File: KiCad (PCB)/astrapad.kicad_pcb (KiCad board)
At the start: 2 copper layers, 106.9 x 53.6 mm, 34 parts, among them J1 OLED_DISPLAY, SW1 SW_Push, SW13 RotaryEncoder_Switch, SW2 SW_Push, SW3 SW_Push, SW5 SW_Push, SW6 SW_Push, SW7 SW_Push, SW8 SW_Push, U1 XIAO-RP2040-DIP

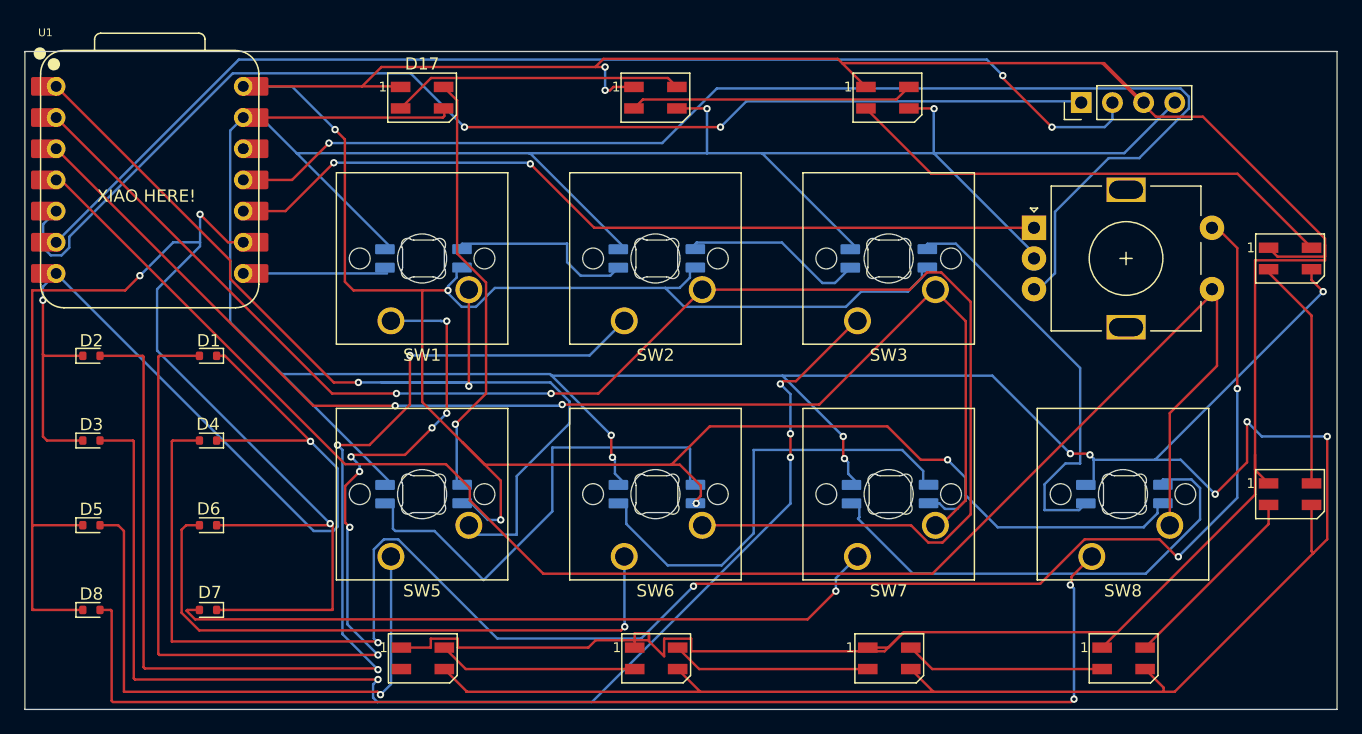
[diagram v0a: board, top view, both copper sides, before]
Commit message: Resized PCB to fit 100mmx100mm limit Turns out the PCB has a max size of 100mmx100mm, mine was 106x59. I resized it though so we good now
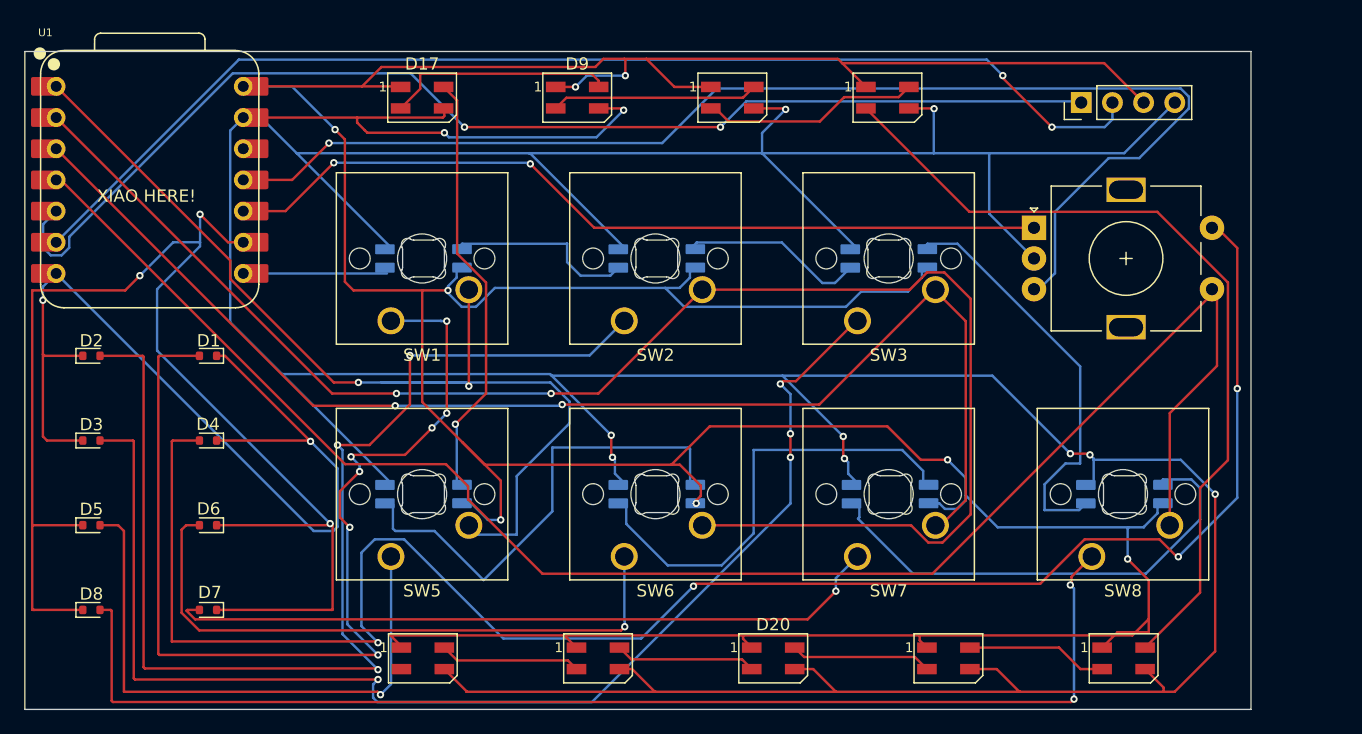
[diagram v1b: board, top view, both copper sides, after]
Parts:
- removed D21: WS2812B, LED_SMD:LED_SK6812MINI_PLCC4_3.5x3.5mm_P1.75mm
- added D9: WS2812B, LED_SMD:LED_SK6812MINI_PLCC4_3.5x3.5mm_P1.75mm, F.Cu at (45.0, 3.76)
- moved D20 53.2 mm to (61.0, 49.4)
- moved D18 6.26 mm to (57.6, 3.76)
- moved D23 4.82 mm to (75.2, 49.4)
- moved D24 4.74 mm to (46.7, 49.4)
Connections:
- D18 pad 4: Net-(D17-DOUT) -> Net-(D18-DIN)
- D20 pad 4: Net-(D19-DOUT) -> Net-(D20-DIN)
- D22 pad 4: Net-(D21-DOUT) -> Net-(D19-DOUT)
- D23 pad 2: Net-(D23-DOUT) -> Net-(D20-DIN)
- D24 pad 4: Net-(D23-DOUT) -> Net-(D20-DOUT)
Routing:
- net +5V: track 410.1 -> 352.5 mm, vias 7 -> 8
- net Net-(D19-DOUT): track 41.0 -> 67.9 mm
- net Net-(D18-DIN): track 0.00 -> 16.9 mm
- net Net-(D23-DOUT): track 16.2 -> 0.00 mm
- net GND: track 426.7 -> 410.6 mm, vias 12 -> 11
- net Net-(D21-DOUT): track 15.8 -> 0.00 mm
- net Net-(D20-DIN): track 0.00 -> 11.5 mm
- net Net-(D20-DOUT): track 19.3 -> 11.5 mm
- net Net-(D18-DOUT): track 23.1 -> 17.8 mm
- net Net-(D17-DOUT): track 23.8 -> 18.8 mm
- net Net-(D22-DOUT): track 16.3 -> 11.5 mm
- net Net-(D24-DOUT): track 16.2 -> 11.5 mm
- net Net-(D4-A): track 145.8 -> 147.1 mm
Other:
- board size 106.9 x 53.6 mm -> 99.9 x 53.6 mm
